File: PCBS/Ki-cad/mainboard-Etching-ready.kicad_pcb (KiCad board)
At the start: 2 copper layers, 99.1 x 81.3 mm, 34 parts, among them IC1 74HC86, J1 SENSORS, J2 CONN_06SILK_FEMALE_PTH, J3 CONN_06SILK_FEMALE_PTH, J4 POWER, J5 SERIAL, M1 Left Motor, M2 Right Motor, U1 Arduino_Nano, U2 TB6612FNG-Module

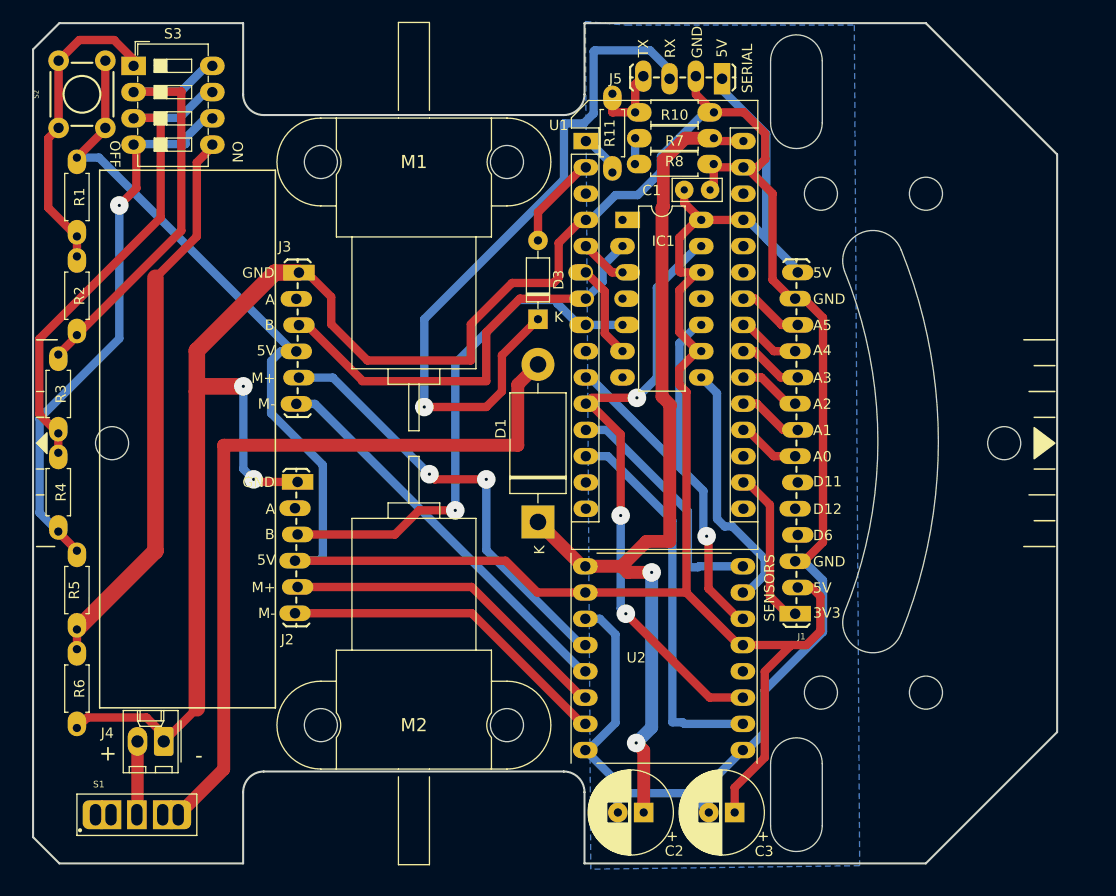
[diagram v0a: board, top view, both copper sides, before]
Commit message: ki cad files update according to easier to solder versions
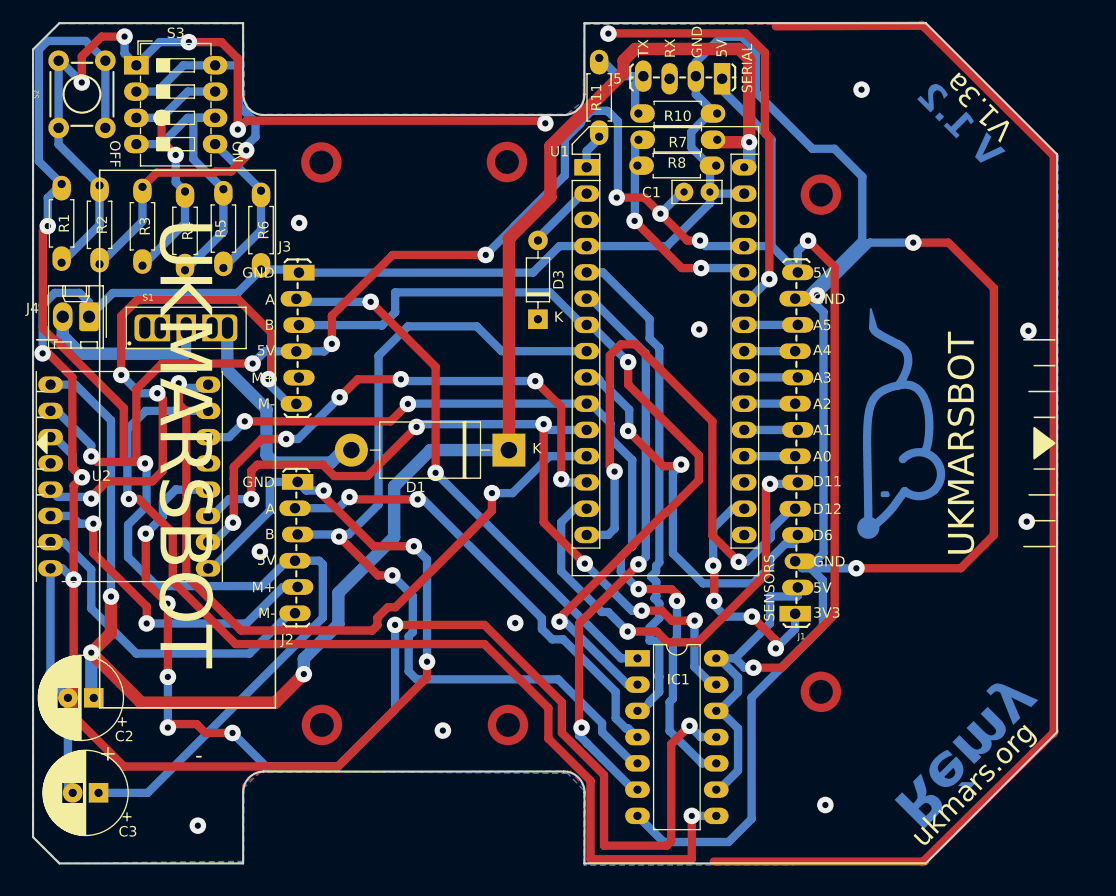
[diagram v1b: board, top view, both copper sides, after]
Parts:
- removed H1, H2, H3, H4, H5, H6: MountingHole, ukmarsbot:MountingHole_3.2mm_M3_clearance
- removed M1: Left Motor, ukmarsbot:MINI-METAL-GEARMOTOR-WITH-BRACKET
- removed M2: Right Motor, ukmarsbot:MINI-METAL-GEARMOTOR-WITH-BRACKET
- moved C3 61.6 mm to (74.5, 138.8)
- moved U2 54.6 mm to (77.5, 108.2)
- moved C2 54.3 mm to (74.0, 129.6)
- moved R6 47.8 mm to (90.2, 88.2)
- moved S1 47.3 mm to (83.0, 93.8)
- moved IC1 42.4 mm to (126.6, 125.8)
- moved J4 41.7 mm to (73.6, 92.8)
- moved R5 37.7 mm to (86.6, 80.4)
- moved R4 28.1 mm to (82.9, 88.3)
- moved R3 18.1 mm to (78.7, 87.8)
- moved D1 7.50 mm to (114.2, 105.7), turned to 180 degrees
- moved R2 7.20 mm to (74.6, 87.7)
- moved R11 3.69 mm to (122.9, 67.7)
- moved R1 2.95 mm to (70.9, 87.5)
- moved U1 2.54 mm to (121.7, 78.3)
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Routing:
- net GND: track 270.4 -> 426.7 mm, vias 2 -> 19
- net //RIGHT_DIR: track 0.00 -> 118.9 mm, vias 0 -> 7
- net 5V: track 221.0 -> 336.5 mm, vias 0 -> 11
- net /FUNCTION_SELECT: track 30.0 -> 126.2 mm, vias 0 -> 7
- net //LEFT_DIR: track 24.9 -> 99.7 mm, vias 0 -> 2
- net /V_BATT: track 88.8 -> 162.3 mm, vias 2 -> 4
- net /RXD_BT: track 67.9 -> 0.00 mm, vias 1 -> 0
- net /EMITTER_B: track 0.00 -> 56.9 mm, vias 0 -> 2
- net /LEFT_A: track 0.00 -> 53.4 mm, vias 0 -> 2
- net /SW_PWR: track 74.6 -> 22.5 mm
- net /LEFT_PWM: track 23.9 -> 71.4 mm, vias 0 -> 2
- net /RIGHT_CLK_A: track 9.09 -> 55.5 mm, vias 0 -> 2
- net /RIGHT_A: track 0.00 -> 45.3 mm, vias 0 -> 2
- net /LEFT_CLK_A: track 4.88 -> 49.8 mm
- net /EMITTER_A: track 0.00 -> 44.8 mm, vias 0 -> 2
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- added copper zone on F.Cu, net GND
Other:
- outline, holes or cut-outs redrawn
- board text added: "Rémy"
- board text added: "UKMARSBOT"
- board text added: "V 1.2"
- board text added: "V1.3a"
- board text added: "ukmars.org"
- board text removed: "Ratatouille"
- board text removed: "V1"
